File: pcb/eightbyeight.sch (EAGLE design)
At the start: 131 parts, among them CON1 USB_MICROSMT+THRUHULE, Q1 16MHz, SW1 SWITCH_SPDT, SW2 BRIGHTNESS, U1 MK20D--VFM5, U2 ICN2026, U3 74138, U4 ICN2026, U5 MIC5219 3.3V, U8 MMA8653FC

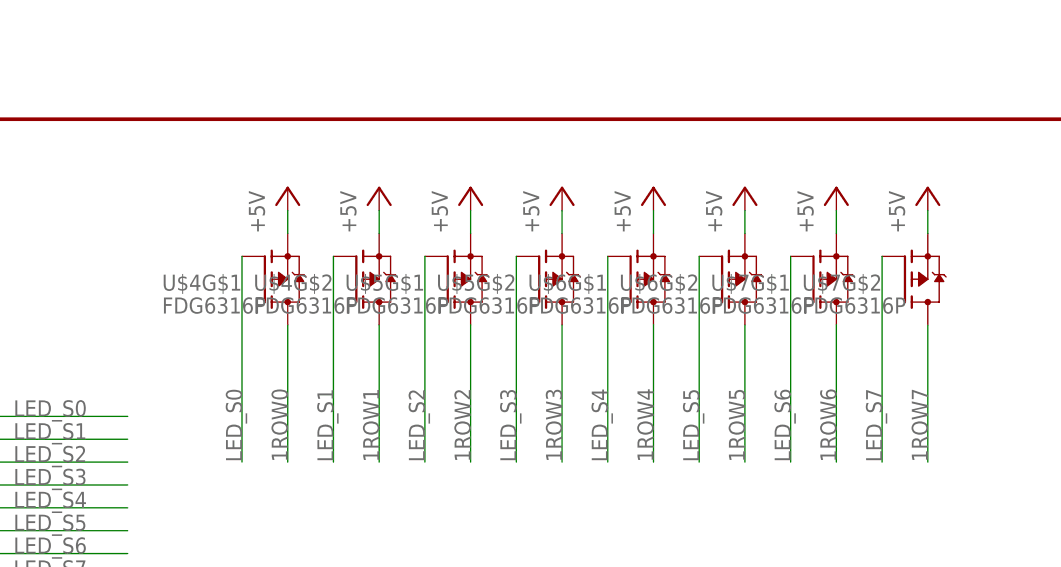
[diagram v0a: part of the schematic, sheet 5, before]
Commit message: Clean up label placements on PCB
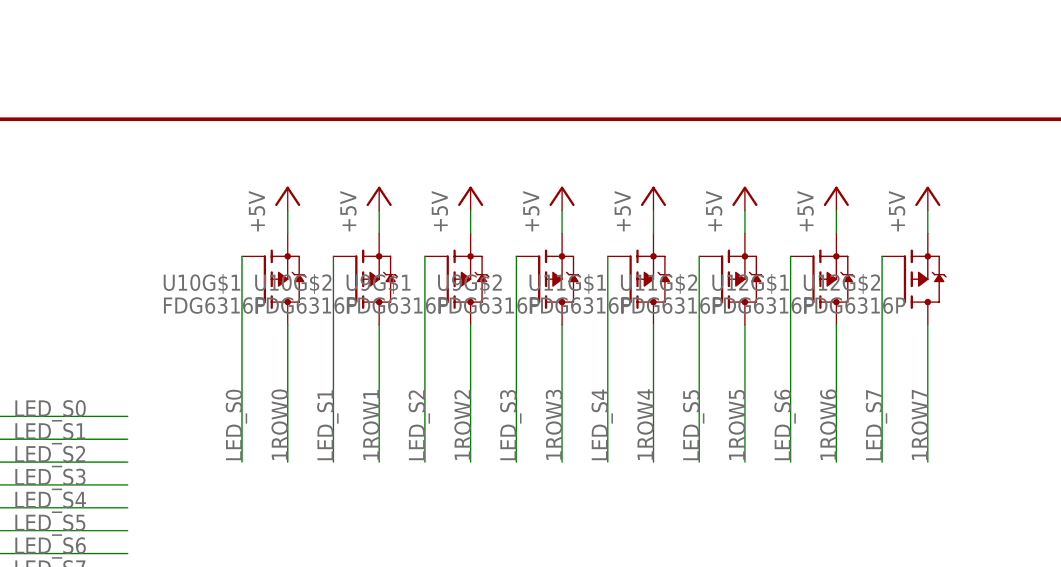
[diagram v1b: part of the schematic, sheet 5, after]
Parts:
- renumbered L4 to L1, U$1 to U6, U$3 to BAT, U$4 to U10, U$5 to U9, U$6 to U11, U$7 to U12
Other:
- note added: "EightByEight PCB Notes/Changelog Revision A: -Power circuit doesn't power device when charging, need to add bypass diodes to connect USB_5V to +5V. Should also add diode in-line with output from regulator so they don't conflict. Revision B: TODO: -Connect gpo0/reset on the ESP to the ARM, so we can initiate firmware updates automatically? -Connect arm to I2C bus for LED control sans serial? -Test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"
- note removed: "EightByEight PCB Notes/Changelog Revision A: -Power circuit doesn't power device when charging, need to add bypass diodes to connect USB_5V to +5V. Should also add diode in-line with output from regulator so they don't conflict. Revision B:"

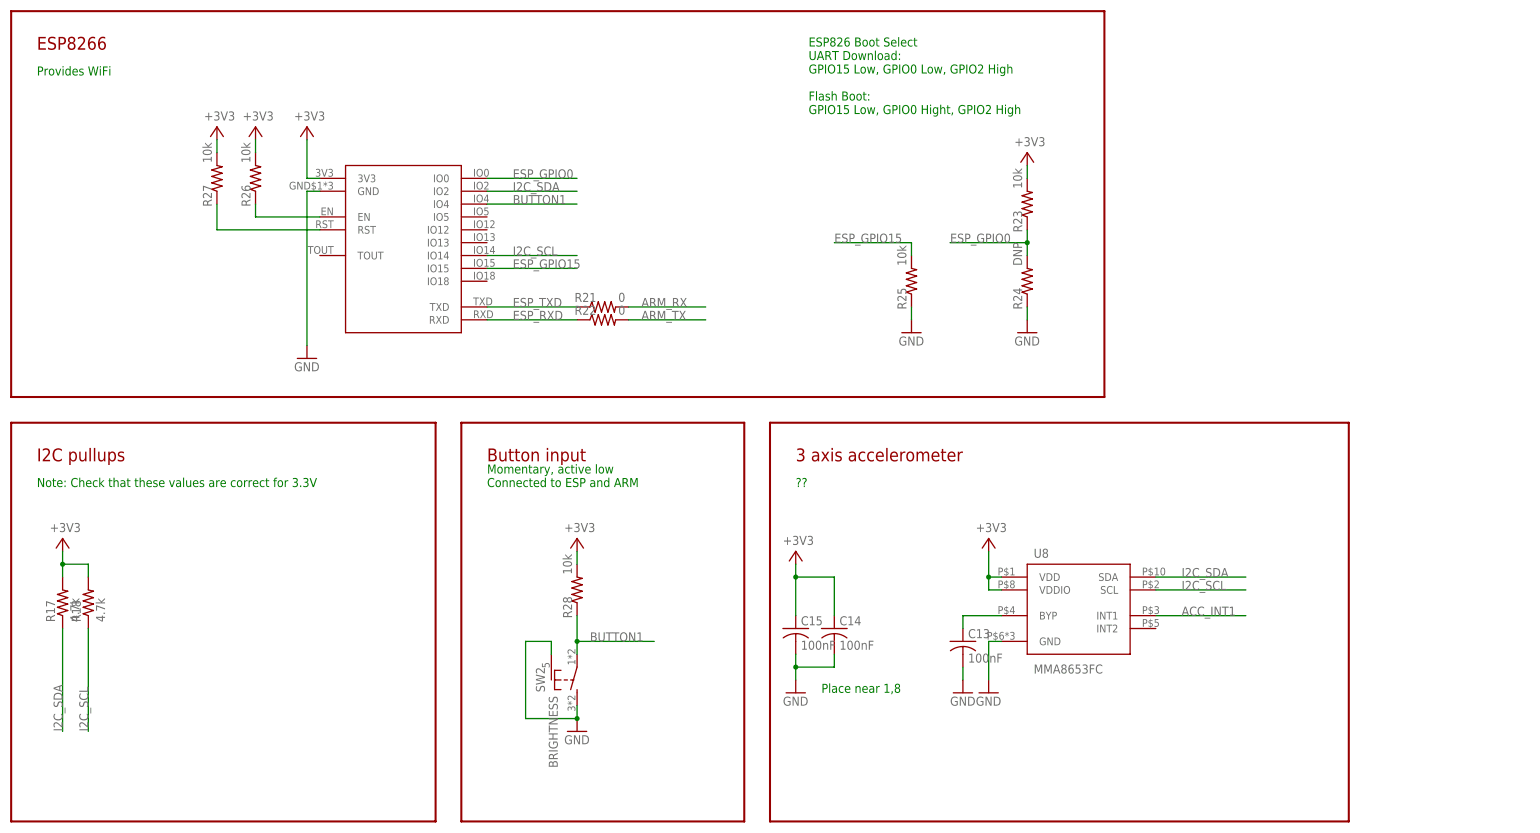
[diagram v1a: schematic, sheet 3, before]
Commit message: Routing changes on PCB, cleanup
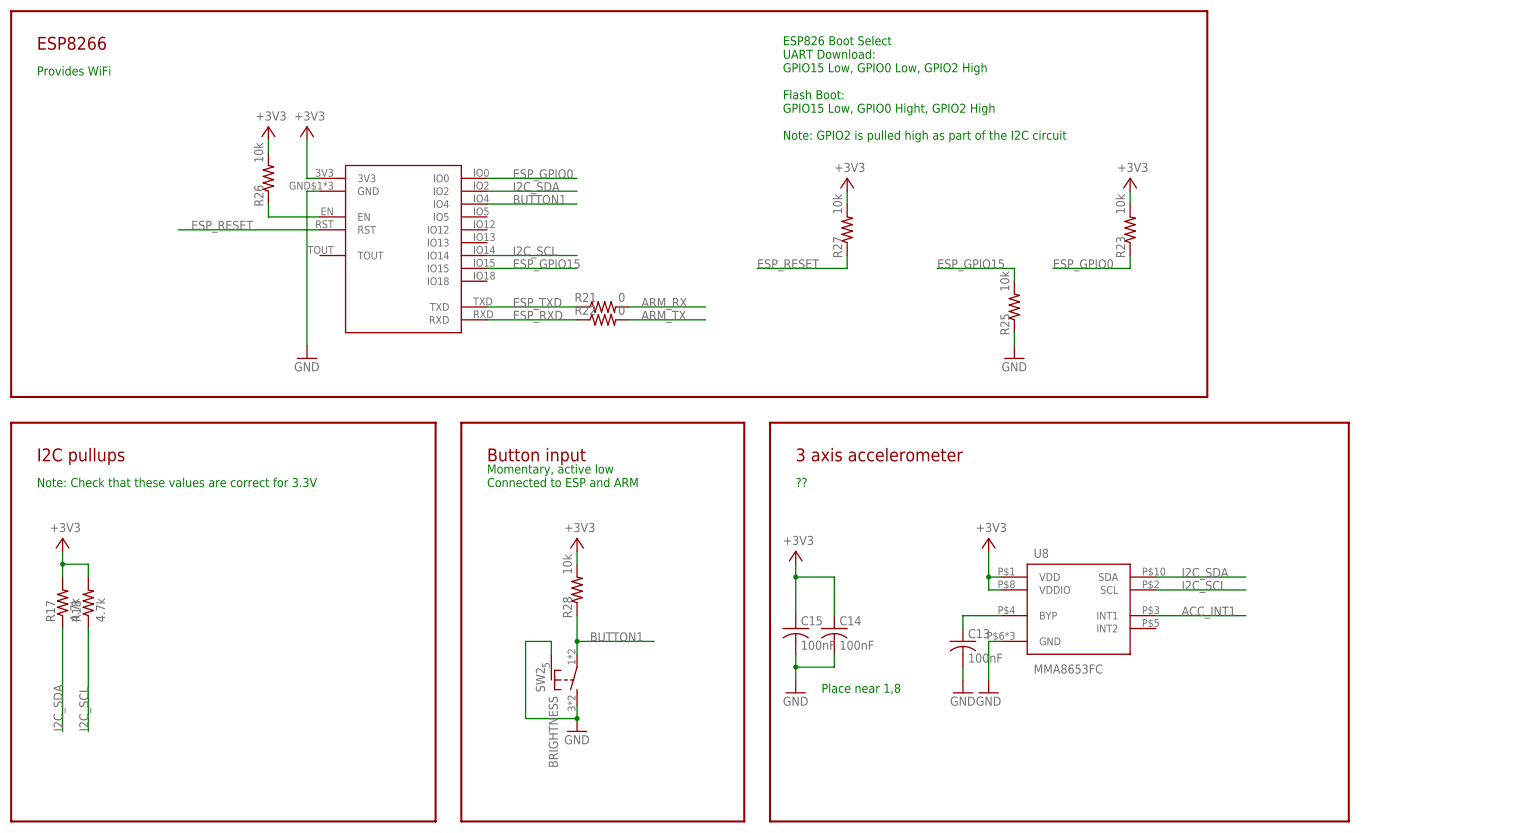
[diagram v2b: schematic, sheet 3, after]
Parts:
- removed R24: DNP, adafruit:R-US_R0402
- added D2, D3: RB161M-20, adafruit:DIODESOD-123
- added R11: 50, adafruit:R-US_R0805
- U1: value MK20D--VFM5 -> MK20DN64VFM5
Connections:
- net N$8 renamed ESP_ENABLE
- removed net N$11: R27.1, U6.RST
- new net BOOST_5V: C9.1, D2.A, U$8.OUT
- new net ESP_RESET: R27.1, U1.PTB0, U6.RST
- new net N$1: D2.C, D3.C, SW1.S
- net +5V: now also SW1.P; no longer SW1.S
- net ESP_GPIO0: now also U1.PTB1; no longer R24.2
- net GND: now also R11.1; no longer R24.1
- net N$4: now also R11.2, SW1.O; no longer C9.1, SW1.P, U$8.OUT
- net USB_5V: now also D3.A
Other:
- note added: "Drain resistor to protect againt rapid on/off power cycles"
- note added: "ESP826 Boot Select UART Download: GPIO15 Low, GPIO0 Low, GPIO2 High Flash Boot: GPIO15 Low, GPIO0 Hight, GPIO2 High Note: GPIO2 is pulled high as part of the I2C circuit"
- note added: "EightByEight PCB Notes/Changelog Revision A: -Mod required to power over USB Revision B: -Add diodes to enable power from USB -Connect ESP reset and boot select pins to ARM for auto-programming TODO: -Connect arm to I2C bus for accelerometer, potential ESP8266 control -Connect button directly to ARM for application and DFU hooks -Test power supply for ESP8266, is something bigger required? -Hook 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"
- note added: "Pin assignments for matrix output: LED_DAT + LED_CLK need to be together on a unique port LED_ROW_* and LED_STB need to be together on a unique port LED_OE needs to be on a pin with FTM capability"
- note added: "Power switch"
- note added: "Powers device from USB or battery"
- note removed: "ESP826 Boot Select UART Download: GPIO15 Low, GPIO0 Low, GPIO2 High Flash Boot: GPIO15 Low, GPIO0 Hight, GPIO2 High"
- note removed: "EightByEight PCB Notes/Changelog Revision A: -Power circuit doesn't power device when charging, need to add bypass diodes to connect USB_5V to +5V. Should also add diode in-line with output from regulator so they don't conflict. Revision B: TODO: -Connect gpo0/reset on the ESP to the ARM, so we can initiate firmware updates automatically? -Connect arm to I2C bus for LED control sans serial? -Test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"
- note removed: "Pin assignments: LED_DAT + LED_CLK need to be on a unique port LED_ROW_A, LED_ROW_B, and LED_STB need to be on a unique port LED_OE needs to be on a unique port (?)"
- moved on the sheet: R23, R25, R26, R27, SW1

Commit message: Continue implementing changes from TODO
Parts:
- removed R21, R22: 0, adafruit:R-US_R0402
- added ANALOG_IN, TP1, TP2, TP3: PTR1B2,54, testpad:PTR1B2,54
- added R12: 10k, adafruit:R-US_R0402
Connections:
- removed net ESP_RXD: R22.1, U6.RXD
- removed net ESP_TXD: R21.1, U6.TXD
- removed net I2C_SDA: R17.1, U6.IO2, U8.SDA
- new net ARM_RX1: R12.1, R17.1, U1.PTC3, U6.IO2, U8.SDA
- new net ESP_EXP_1: TP3.TP, U6.IO5
- new net ESP_EXP_2: TP2.TP, U6.IO12
- new net ESP_EXP_3: TP1.TP, U6.IO18
- new net ESP_TOUT: ANALOG_IN.TP, U6.TOUT
- net +3V3: now also R12.2
- net ACC_INT1: now also U6.IO13
- net ARM_RX: now also U6.TXD; no longer R21.2
- net ARM_TX: now also U6.RXD; no longer R22.2
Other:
- note added: "ESP826 Boot Select UART Download: GPIO15 Low, GPIO0 Low, GPIO2 High Flash Boot: GPIO15 Low, GPIO0 Hight, GPIO2 High"
- note added: "EightByEight PCB Notes/Changelog Revision A: -Mod required to power over USB Revision B: -Add diodes to enable power from USB -Connect ESP reset and boot select pins to ARM for auto-programming -Connect ESP TX1 pin to ARM for LED control or modeswitch TODO: -Add jumper pad for entering boot mode on ARM processor -Test power supply for ESP8266, is something bigger required? -Hook LED_OE or similar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"
- note added: "Extra IO"
- note added: "Unused pins from the ESP8266"
- note removed: "ESP826 Boot Select UART Download: GPIO15 Low, GPIO0 Low, GPIO2 High Flash Boot: GPIO15 Low, GPIO0 Hight, GPIO2 High Note: GPIO2 is pulled high as part of the I2C circuit"
- note removed: "EightByEight PCB Notes/Changelog Revision A: -Mod required to power over USB Revision B: -Add diodes to enable power from USB -Connect ESP reset and boot select pins to ARM for auto-programming TODO: -Connect arm to I2C bus for accelerometer, potential ESP8266 control -Connect button directly to ARM for application and DFU hooks -Test power supply for ESP8266, is something bigger required? -Hook 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"
- moved on the sheet: R23, R25, R26, R27
